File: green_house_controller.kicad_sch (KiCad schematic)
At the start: 7 parts, among them J2 Screw_Terminal_01x05, J3 USB_B_Mini, J4 Screw_Terminal_01x06

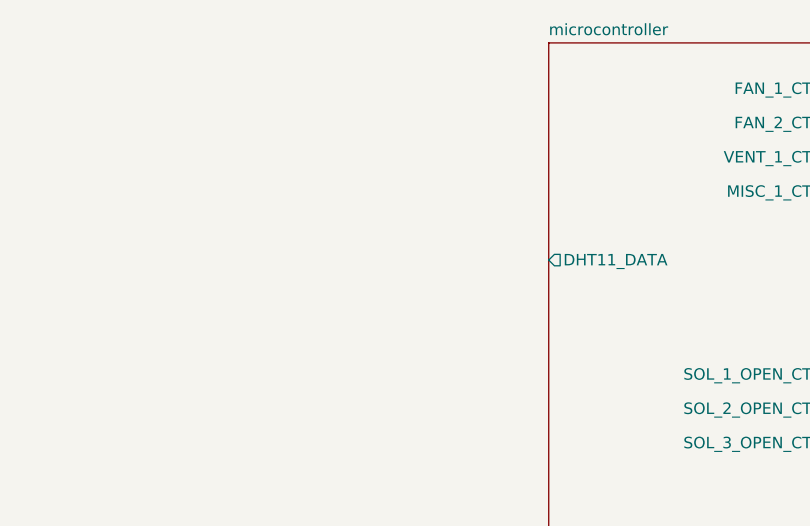
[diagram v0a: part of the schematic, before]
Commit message: Added connector for temperature sensor. Started to route board.
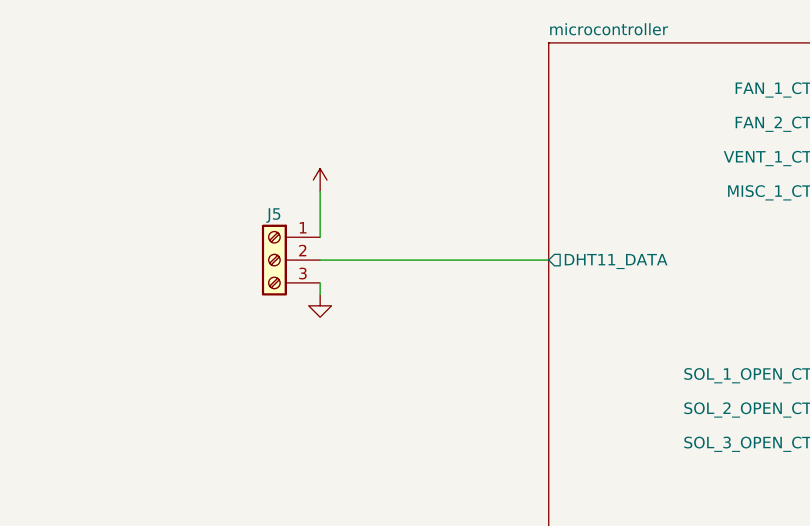
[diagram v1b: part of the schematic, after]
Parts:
- added J5: (no value), symbol Connector:Screw_Terminal_01x03
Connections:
- net GND: now also J5.3 (Pin_3)
- net microcontroller/DHT11_DATA: now also J5.2 (Pin_2)
- new net +3V3: J5.1 (Pin_1)
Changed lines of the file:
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@@
+    (stroke (width 0) (type default) (color 0 0 0 0))
+  )
+  (wire (pts (xy 81.28 66.04) (xy 106.68 66.04))
     (stroke (width 0) (type default) (color 0 0 0 0))
   )
@@
     (stroke (width 0) (type default) (color 0 0 0 0))
   )
+  (wire (pts (xy 81.28 68.58) (xy 81.28 69.85))
+    (stroke (width 0) (type default) (color 0 0 0 0))
+  )
   (wire (pts (xy 147.32 139.7) (xy 153.67 139.7))
     (stroke (width 0) (type default) (color 0 0 0 0))
@@
   )
   (wire (pts (xy 199.39 139.7) (xy 187.96 139.7))
+    (stroke (width 0) (type default) (color 0 0 0 0))
+  )
+  (wire (pts (xy 81.28 58.42) (xy 81.28 63.5))
     (stroke (width 0) (type default) (color 0 0 0 0))
   )
@@
     )
   )
+  (symbol (lib_id "power:GND") (at 81.28 69.85 0) (unit 1)
+    (in_bom yes) (on_board yes) (fields_autoplaced)
+    (property "Reference" "#PWR071" (id 0) (at 81.28 76.2 0)
+      (effects (font (size 1.27 1.27)) hide)
+    )
+    (property "Value" "" (id 1) (at 81.28 74.93 0))
+    (property "Footprint" "" (id 2) (at 81.28 69.85 0)
+      (effects (font (size 1.27 1.27)) hide)
+    )
+    (property "Datasheet" "" (id 3) (at 81.28 69.85 0)
+      (effects (font (size 1.27 1.27)) hide)
+    )
+    (pin "1")
+  )
   (symbol (lib_id "Connector:Screw_Terminal_01x05") (at 207.01 53.34 0) (unit 1)
     (in_bom yes) (on_board yes) (fields_autoplaced)
@@
       (effects (font (size 1.27 1.27)) hide)
     )
+  )
+  (symbol (lib_id "power:+3V3") (at 81.28 58.42 0) (unit 1)
+    (in_bom yes) (on_board yes) (fields_autoplaced)
+    (property "Reference" "#PWR01" (id 0) (at 81.28 62.23 0)
+      (effects (font (size 1.27 1.27)) hide)
+    )
+    (property "Value" "" (id 1) (at 81.28 53.34 0))
+    (property "Footprint" "" (id 2) (at 81.28 58.42 0)
+      (effects (font (size 1.27 1.27)) hide)
+    )
+    (property "Datasheet" "" (id 3) (at 81.28 58.42 0)
+      (effects (font (size 1.27 1.27)) hide)
+    )
+    (pin "1")
   )
   (symbol (lib_id "Connector:Screw_Terminal_01x06") (at 207.01 85.09 0) (unit 1)
@@
     (pin "6")
   )
+  (symbol (lib_id "Connector:Screw_Terminal_01x03") (at 76.2 66.04 0) (mirror y) (unit 1)
+    (in_bom yes) (on_board yes)
+    (property "Reference" "J5" (id 0) (at 76.2 60.96 0))
+    (property "Value" "" (id 1) (at 63.5 66.04 0))
+    (property "Footprint" "" (id 2) (at 76.2 66.04 0)
+      (effects (font (size 1.27 1.27)) hide)
+    )
+    (property "Datasheet" "~" (id 3) (at 76.2 66.04 0)
+      (effects (font (size 1.27 1.27)) hide)
+    )
+    (pin "1")
+    (pin "2")
+    (pin "3")
+  )
   (symbol (lib_id "Mechanical:MountingHole") (at 19.05 187.96 0) (unit 1)
     (in_bom yes) (on_board yes) (fields_autoplaced)
@@
   )
   (symbol_instances
-    (path "/00000000-0000-0000-0000-0000625b126e/00000000-0000-0000-0000-0000625b59c2"
-      (reference "#PWR01") (unit 1) (value "+3.3V") (footprint "")
+    (path "/a374d398-d556-4b16-bf91-a17b3eb16fa6"
+      (reference "#PWR01") (unit 1) (value "+3V3") (footprint "")
     )
     (path "/00000000-0000-0000-0000-0000625b126e/00000000-0000-0000-0000-0000625b6e3f"
@@
       (reference "#PWR070") (unit 1) (value "GND") (footprint "")
     )
-    (path "/00000000-0000-0000-0000-0000625b126e/00000000-0000-0000-0000-0000625c180e"
-      (reference "#PWR0101") (unit 1) (value "+3.3V") (footprint "")
+    (path "/57548200-abe4-438a-9a8e-527562d027da"
+      (reference "#PWR071") (unit 1) (value "GND") (footprint "")
+    )
+    (path "/00000000-0000-0000-0000-0000625b126e/9fca9f38-313d-4d63-b508-772bf3dd10b0"
+      (reference "#PWR0101") (unit 1) (value "+3V3") (footprint "")
     )
     (path "/00000000-0000-0000-0000-0000625b57c4/0f34061d-d120-4957-8724-c661dae5e1c6"
       (reference "#PWR0102") (unit 1) (value "GND") (footprint "")
     )
+    (path "/00000000-0000-0000-0000-0000625b126e/13db70a7-fc45-4937-a5c8-51c8779c7698"
+      (reference "#PWR0103") (unit 1) (value "+3V3") (footprint "")
+    )
     (path "/00000000-0000-0000-0000-0000625b126e/00000000-0000-0000-0000-0000625b6d4b"
       (reference "C1") (unit 1) (value "0.1uF") (footprint "Capacitor_SMD:C_0805_2012Metric")
@@
       (reference "J4") (unit 1) (value "Screw_Terminal_01x06") (footprint "Connector_Phoenix_MC_HighVoltage:PhoenixContact_MCV_1,5_6-G-5.08_1x06_P5.08mm_Vertical")
     )
+    (path "/c3a80e6a-879a-435d-80c2-69f2fc71263b"
+      (reference "J5") (unit 1) (value "Screw_Terminal_01x03") (footprint "Connector_Phoenix_MC_HighVoltage:PhoenixContact_MCV_1,5_3-G-5.08_1x03_P5.08mm_Vertical")
+    )
     (path "/00000000-0000-0000-0000-0000625b57c4/805c6998-aa25-41d5-902d-bb6054c83736"

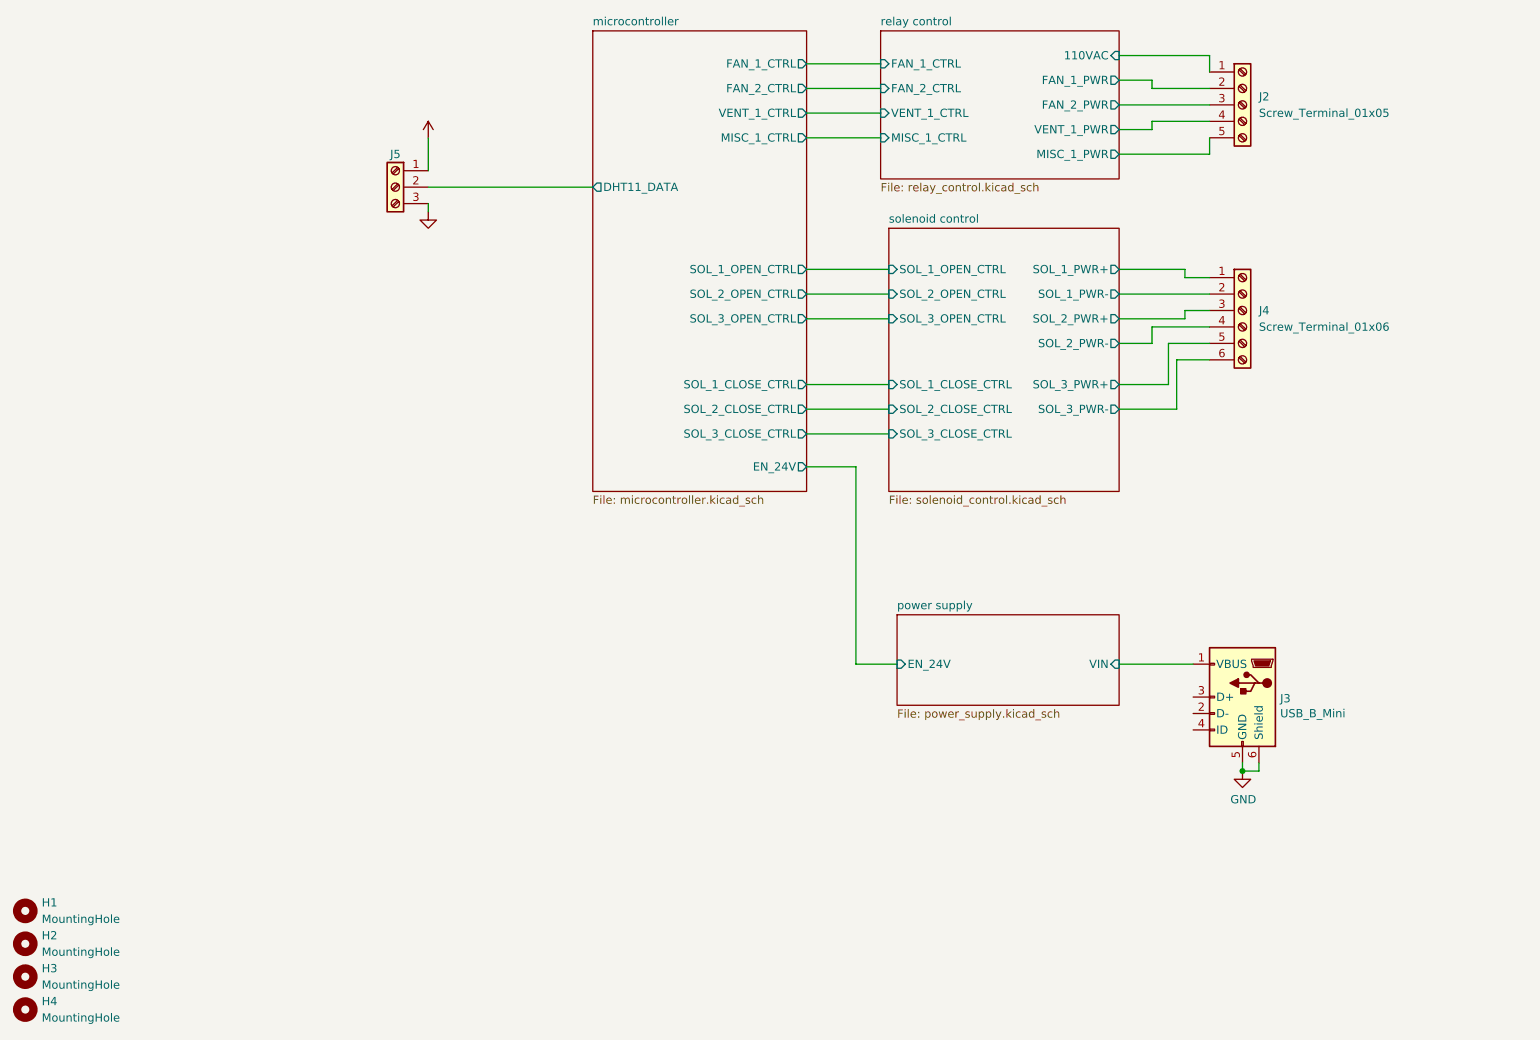
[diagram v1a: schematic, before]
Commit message: Added clamping diode for 24V net.
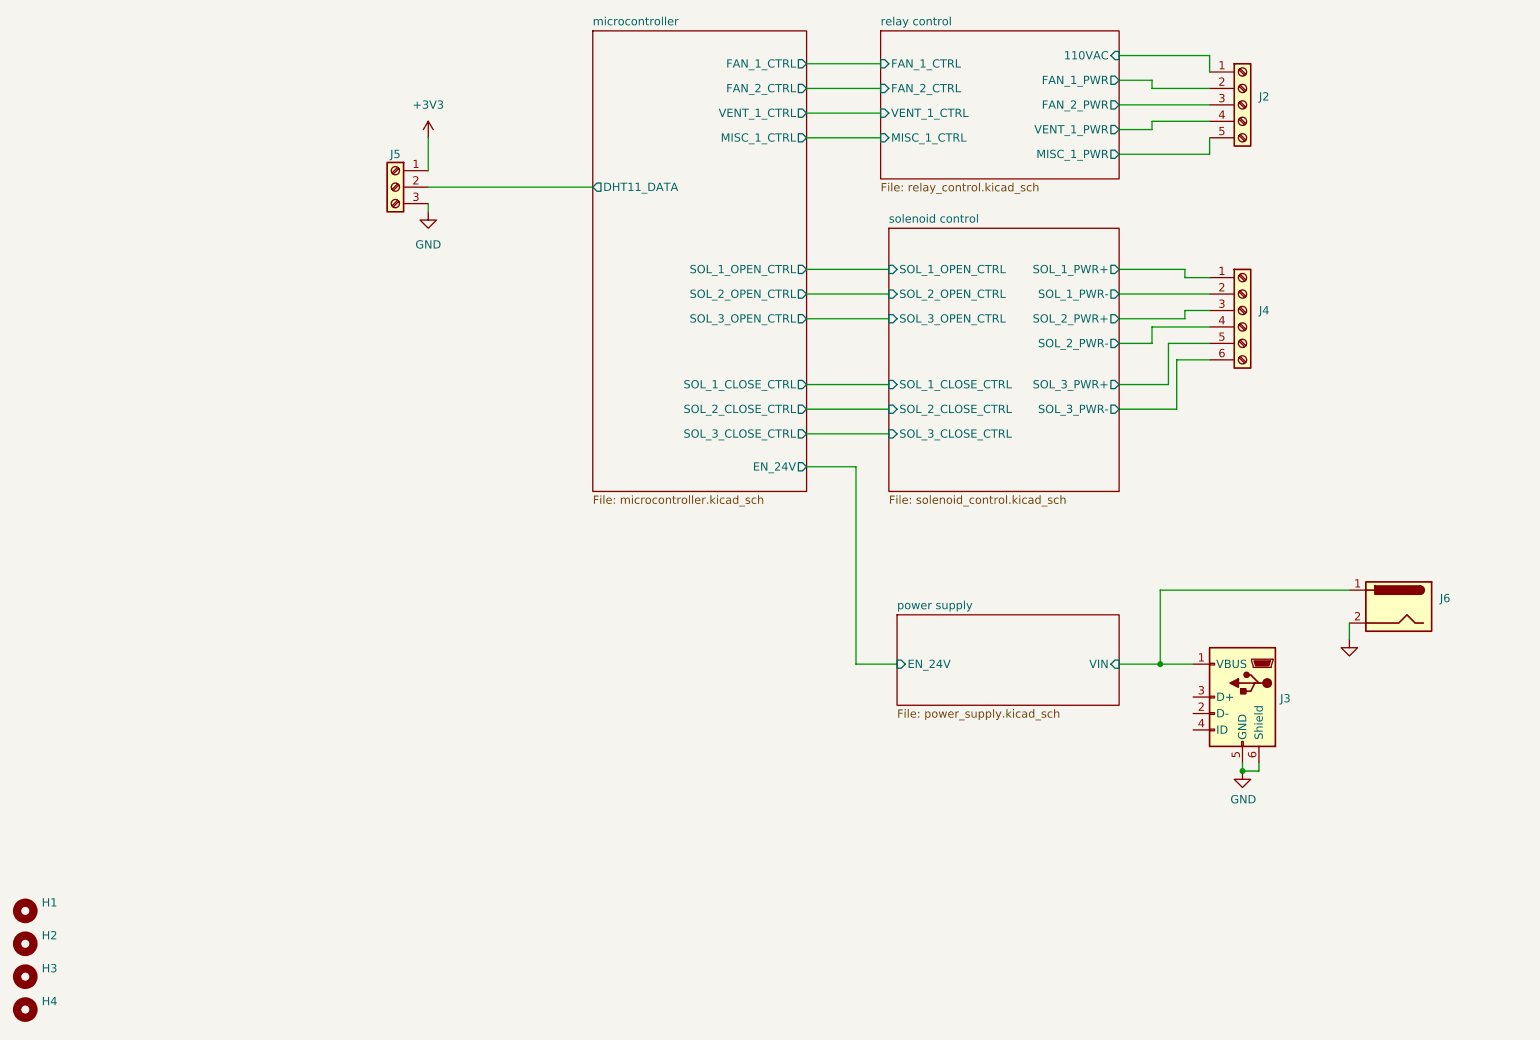
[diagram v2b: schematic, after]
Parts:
- added J6: (no value), symbol Connector:Barrel_Jack
- H1, H2, H3, H4: value MountingHole -> (none); footprint MountingHole:MountingHole_3.2mm_M3 -> (none)
- J2: value Screw_Terminal_01x05 -> (none); footprint Connector_Phoenix_MC_HighVoltage:PhoenixContact_MCV_1,5_5-G-5.08_1x05_P5.08mm_Vertical -> (none)
- J3: value USB_B_Mini -> (none); footprint Connector_USB:USB_Mini-B_Lumberg_2486_01_Horizontal -> (none)
- J4: value Screw_Terminal_01x06 -> (none); footprint Connector_Phoenix_MC_HighVoltage:PhoenixContact_MCV_1,5_6-G-5.08_1x06_P5.08mm_Vertical -> (none)
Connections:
- net GND: now also J6.2
- net power supply/VIN: now also J6.1

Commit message: Continued with layout.
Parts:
- removed J2: (no value), symbol Connector:Screw_Terminal_01x05
- added J2: (no value), symbol Connector:Screw_Terminal_01x10
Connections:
- net relay control/110VAC: now also J2.1 (Pin_1)
- net relay control/FAN_1_PWR: now also J2.3 (Pin_3)
- net relay control/FAN_2_PWR: now also J2.5 (Pin_5)
- net relay control/MISC_1_PWR: now also J2.9 (Pin_9)
- net relay control/VENT_1_PWR: now also J2.7 (Pin_7)
- new net Earth: J2.10 (Pin_10), J2.2 (Pin_2), J2.4 (Pin_4), J2.6 (Pin_6), J2.8 (Pin_8)
